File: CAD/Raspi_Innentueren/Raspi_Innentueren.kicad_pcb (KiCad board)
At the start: 2 copper layers, 1 part, among them J101 Conn_02x16_Counter_Clockwise

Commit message: -bug: fixed bugs in raspi schematic -mod: added confirm button and additional check button -mod: PWR_EN signals shifted from 3V3 to 12V level via transistor
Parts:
- added C101: 100u/16V, Capacitor_THT:CP_Radial_D8.0mm_P2.50mm, F.Cu at (70.0, 57.5)
- added C102: 100n/16V, Capacitor_THT:C_Rect_L7.2mm_W2.5mm_P5.00mm_FKS2_FKP2_MKS2_MKP2, F.Cu at (76.9, 54.8)
- added D101: D_Small, Diode_THT:D_DO-35_SOD27_P7.62mm_Horizontal, F.Cu at (107.6, 48.4)
- added D102: D_Small, Diode_THT:D_DO-35_SOD27_P7.62mm_Horizontal, F.Cu at (97.8, 48.4)
- added D103: D_Small, Diode_THT:D_DO-35_SOD27_P7.62mm_Horizontal, F.Cu at (88.0, 48.4)
- added D104: rt, LED_THT:LED_D5.0mm_Clear, F.Cu at (266.7, 100.3)
- added D105: gn, LED_THT:LED_D5.0mm_Clear, F.Cu at (266.7, 87.6)
- added J102: Conn_02x20_Odd_Even, Connector_PinSocket_2.54mm:PinSocket_2x20_P2.54mm_Vertical, F.Cu at (114.3, 72.4)
- added Q101: Q_NPN_CBE, Package_TO_SOT_THT:TO-92L_Inline_Wide, F.Cu at (39.1, 82.6)
- added Q102: Q_NPN_CBE, Package_TO_SOT_THT:TO-92L_Inline_Wide, F.Cu at (46.3, 66.6)
- added Q103: Q_NPN_CBE, Package_TO_SOT_THT:TO-92L_Inline_Wide, F.Cu at (53.4, 63.6)
- added Q104: Q_NPN_CBE, Package_TO_SOT_THT:TO-92L_Inline_Wide, F.Cu at (246.4, 119.4)
- added R101: 20k, Resistor_THT:R_Axial_DIN0207_L6.3mm_D2.5mm_P7.62mm_Horizontal, F.Cu at (78.3, 48.7)
- added R102: 39k, Resistor_THT:R_Axial_DIN0207_L6.3mm_D2.5mm_P7.62mm_Horizontal, F.Cu at (68.5, 48.7)
- added R103: 1k, Resistor_THT:R_Axial_DIN0207_L6.3mm_D2.5mm_P7.62mm_Horizontal, F.Cu at (58.7, 48.7)
- added R104: 20k, Resistor_THT:R_Axial_DIN0207_L6.3mm_D2.5mm_P7.62mm_Horizontal, F.Cu at (48.9, 48.7)
- added R105: 39k, Resistor_THT:R_Axial_DIN0207_L6.3mm_D2.5mm_P7.62mm_Horizontal, F.Cu at (107.6, 54.3)
- added R106: 330R, Resistor_THT:R_Axial_DIN0207_L6.3mm_D2.5mm_P7.62mm_Horizontal, F.Cu at (261.6, 110.5)
- added R107: 20k, Resistor_THT:R_Axial_DIN0207_L6.3mm_D2.5mm_P7.62mm_Horizontal, F.Cu at (68.5, 51.7)
- added R108: 39k, Resistor_THT:R_Axial_DIN0207_L6.3mm_D2.5mm_P7.62mm_Horizontal, F.Cu at (78.3, 51.7)
- added R109: 120R, Resistor_THT:R_Axial_DIN0207_L6.3mm_D2.5mm_P7.62mm_Horizontal, F.Cu at (88.0, 51.2)
- added R110: 10k, Resistor_THT:R_Axial_DIN0207_L6.3mm_D2.5mm_P7.62mm_Horizontal, F.Cu at (97.8, 51.2)
- added R111: 1k, Resistor_THT:R_Axial_DIN0207_L6.3mm_D2.5mm_P7.62mm_Horizontal, F.Cu at (107.6, 51.2)
- added R112: 1k, Resistor_THT:R_Axial_DIN0207_L6.3mm_D2.5mm_P7.62mm_Horizontal, F.Cu at (88.0, 54.3)
- added R113: 10k, Resistor_THT:R_Axial_DIN0207_L6.3mm_D2.5mm_P7.62mm_Horizontal, F.Cu at (97.8, 54.3)
- added R114: 1k, Resistor_THT:R_Axial_DIN0207_L6.3mm_D2.5mm_P7.62mm_Horizontal, F.Cu at (58.7, 51.7)
- added R115: 10k, Resistor_THT:R_Axial_DIN0207_L6.3mm_D2.5mm_P7.62mm_Horizontal, F.Cu at (117.3, 51.7)
- added R116: 10k, Resistor_THT:R_Axial_DIN0207_L6.3mm_D2.5mm_P7.62mm_Horizontal, F.Cu at (48.9, 51.7)
- added R117: 1k, Resistor_THT:R_Axial_DIN0207_L6.3mm_D2.5mm_P7.62mm_Horizontal, F.Cu at (117.3, 54.8)
- added R118: 10k, Resistor_THT:R_Axial_DIN0207_L6.3mm_D2.5mm_P7.62mm_Horizontal, F.Cu at (39.2, 51.7)
- added R119: 1k, Resistor_THT:R_Axial_DIN0207_L6.3mm_D2.5mm_P7.62mm_Horizontal, F.Cu at (117.3, 48.7)
- added SW101: SW_Push, Button_Switch_THT:SW_PUSH_6mm, F.Cu at (266.6, 70.4)
- added SW102: SW_Push, Button_Switch_THT:SW_PUSH_6mm, F.Cu at (266.6, 57.7)
- added SW103: SW_Push, Button_Switch_THT:SW_PUSH_6mm, F.Cu at (266.7, 43.2)
- J101: value Conn_02x16_Counter_Clockwise -> Conn_02x16_Letter_AC
- moved J101 44.3 mm to (22.9, 120.7)

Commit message: -mod: layout Raspi Platine fertiggestellt
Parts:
- J102: moved to B.Cu
- moved Q101 139.0 mm to (177.8, 72.4), turned to 270 degrees
- moved R116 132.6 mm to (165.1, 115.6)
- moved R114 128.9 mm to (172.7, 111.8), turned to 180 degrees
- moved R103 117.0 mm to (172.7, 74.9), turned to 180 degrees
- moved Q104 115.6 mm to (130.8, 115.6), turned to 270 degrees
- moved R104 106.8 mm to (147.3, 90.2), turned to 180 degrees
- moved R118 100.6 mm to (116.8, 115.6)
- moved Q103 97.9 mm to (131.0, 123.2), turned to 270 degrees
- moved R109 95.7 mm to (165.1, 108.0)
- moved R102 95.1 mm to (158.8, 78.7), turned to 180 degrees
- moved Q102 94.1 mm to (131.0, 107.6), turned to 270 degrees
- moved SW103 90.4 mm to (217.0, 118.7)
- moved R108 86.2 mm to (158.8, 82.5), turned to 180 degrees
- moved R107 84.7 mm to (147.3, 82.5), turned to 180 degrees
- moved R111 78.6 mm to (172.7, 95.2), turned to 180 degrees
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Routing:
- net GND: track 0.00 -> 348.7 mm
- net +5V: track 0.00 -> 191.4 mm
- net /~T3_PWR_EN~: track 0.00 -> 85.5 mm
- net /~T1_PWR_EN~: track 0.00 -> 77.6 mm
- net +3V3: track 0.00 -> 71.7 mm
- net +12V: track 0.00 -> 70.6 mm
- net /T3_Error: track 0.00 -> 69.9 mm
- net Net-(D101-Pad1): track 0.00 -> 64.3 mm
- net /T2_Error: track 0.00 -> 62.7 mm
- net /T1_Error: track 0.00 -> 61.7 mm
- net /~T2_PWR_EN~: track 0.00 -> 56.6 mm
- net Net-(R114-Pad1): track 0.00 -> 56.5 mm
- net Net-(D105-Pad2): track 0.00 -> 56.2 mm
- net Net-(R111-Pad1): track 0.00 -> 55.4 mm
- net Net-(D104-Pad1): track 0.00 -> 49.5 mm
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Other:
- board outline added: 160 x 100 mm
- board text added: "Backplane"
- board text added: "Front"
- board text added: "Raspi"

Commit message: -mod: raspi stecker nach oben und links verschoben, mountingholes hinzugefügt
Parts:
- added H101: MountingHole, MountingHole:MountingHole_3.2mm_M3, F.Cu at (118.1, 96.5)
- added H102: MountingHole, MountingHole:MountingHole_3.2mm_M3, F.Cu at (176.1, 145.5)
- added H103: MountingHole, MountingHole:MountingHole_3.2mm_M3, F.Cu at (176.1, 96.6)
- added H104: MountingHole, MountingHole:MountingHole_3.2mm_M3, F.Cu at (118.2, 145.5)
- added H105: MountingHole, MountingHole:MountingHole_3.2mm_M3, F.Cu at (118.1, 57.9)
- added H106: MountingHole, MountingHole:MountingHole_3.2mm_M3, F.Cu at (176.1, 57.9)
- moved R106 99.9 mm to (116.8, 78.7), turned to 90 degrees
- moved D101 6.41 mm to (143.7, 69.6)
- moved Q102 6.41 mm to (127.4, 102.3)
- moved R114 6.41 mm to (169.1, 106.5)
- moved C101 6.41 mm to (123.4, 78.5)
- moved Q104 6.41 mm to (127.2, 110.3)
- moved R110 6.41 mm to (113.2, 102.7)
- moved R115 6.41 mm to (113.2, 117.9)
- moved R118 6.41 mm to (113.2, 110.3)
- moved C102 6.41 mm to (123.5, 86.1)
- moved D102 6.41 mm to (143.7, 88.7)
- moved D103 6.41 mm to (143.7, 81.1)
- moved J102 6.41 mm to (123.4, 97.7)
- moved Q103 6.41 mm to (127.4, 117.9)
- moved R101 6.41 mm to (143.7, 73.4)
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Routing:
- net +5V: track 191.4 -> 85.4 mm
- net Net-(D104-Pad2): track 6.35 -> 108.0 mm
- net GND: track 348.7 -> 342.6 mm
- net /~T3_PWR_EN~: track 85.5 -> 79.7 mm
- net /T3_Error: track 69.9 -> 64.1 mm
- net /~T2_PWR_EN~: track 56.6 -> 50.8 mm
- net Net-(R111-Pad1): track 55.4 -> 61.2 mm
- net Net-(R114-Pad1): track 56.5 -> 60.7 mm
- net /T1_Error: track 61.7 -> 58.0 mm
- net Net-(D104-Pad1): track 49.5 -> 52.8 mm
- net /~T1_PWR_EN~: track 77.6 -> 76.2 mm
- net Net-(D105-Pad2): track 56.2 -> 57.6 mm
- net /T2_Error: track 62.7 -> 61.3 mm
- net +12V: track 70.6 -> 69.3 mm
- net Net-(D101-Pad1): track 64.3 -> 65.0 mm

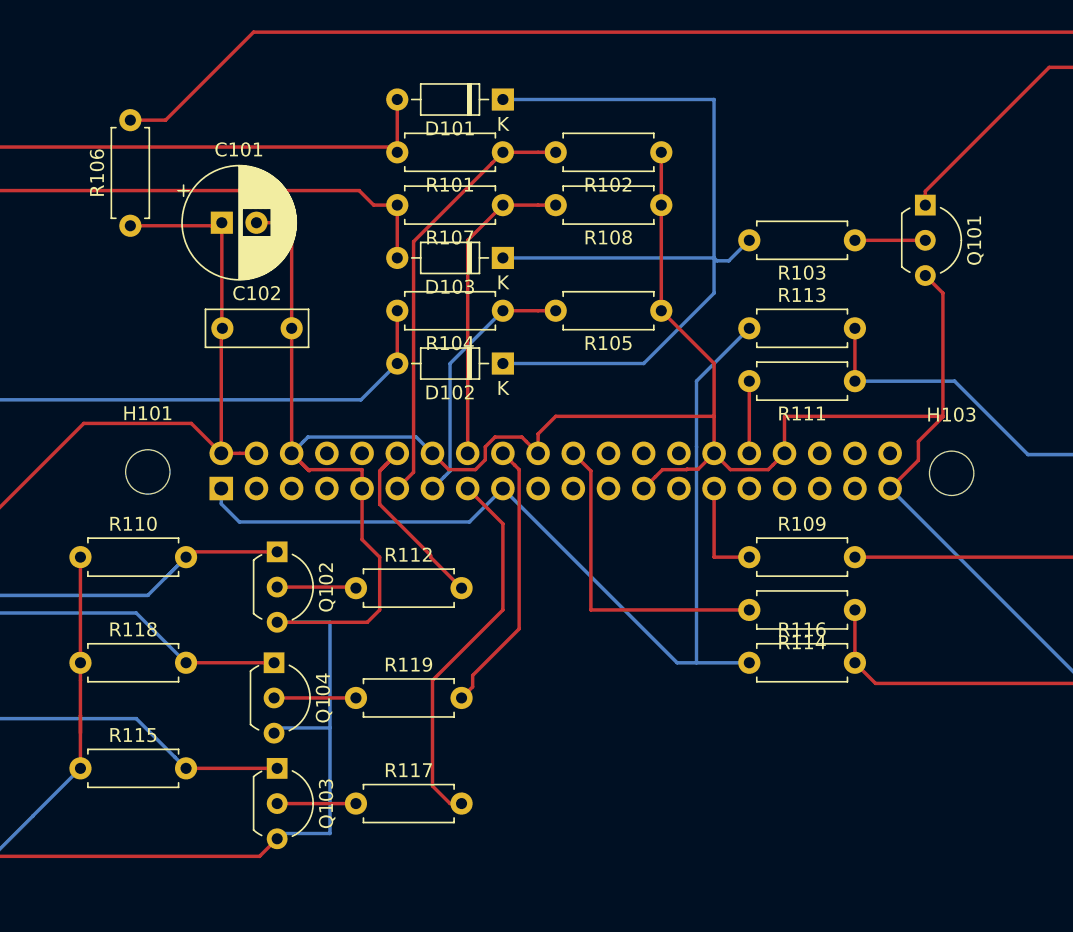
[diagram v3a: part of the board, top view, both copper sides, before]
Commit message: -mod: update shield layout
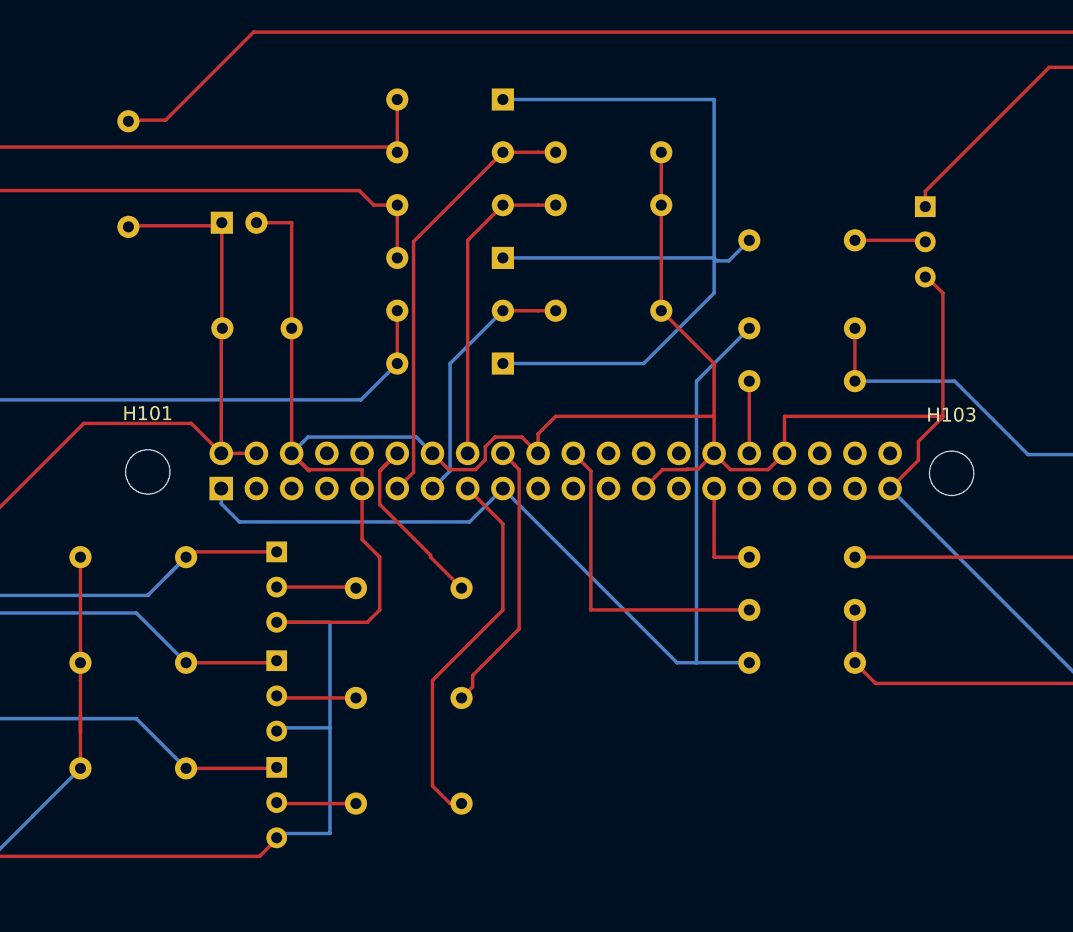
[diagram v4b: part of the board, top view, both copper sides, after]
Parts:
- C101, C102, D101, D102, D103, Q101, Q102, Q103, Q104, R101, R102, R103, R104, R105, R106, R107, R108, R109, R110, R111, R112, R113, R114, R115, R116, R117, R118, R119: moved to B.Cu
- moved Q104 0.24 mm to (127.4, 110.1)
- moved R106 0.16 mm to (116.7, 78.8)
- moved Q101 0.11 mm to (174.2, 77.4)
- moved Q103 0.08 mm to (127.4, 117.8)
